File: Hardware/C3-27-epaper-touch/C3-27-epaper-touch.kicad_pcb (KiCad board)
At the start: 4 copper layers, 70.2 x 71 mm, 63 parts, among them J1 AFC24-S24FIC-00, J2 USB_C_Programming, J3 Conn_01x06, J4 Conn_01x06_Female, J5 Groove sensor, Q1 Si1308, Q2 BC817, Q3 BC817, U1 ESP32-C3-WROOM-02-N4, U2 CP2102N-A02-GQFN28R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

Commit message: C3 PCB update RES label
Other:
- board text added: "0.47Ω"
- board text removed: "4.7Ω"

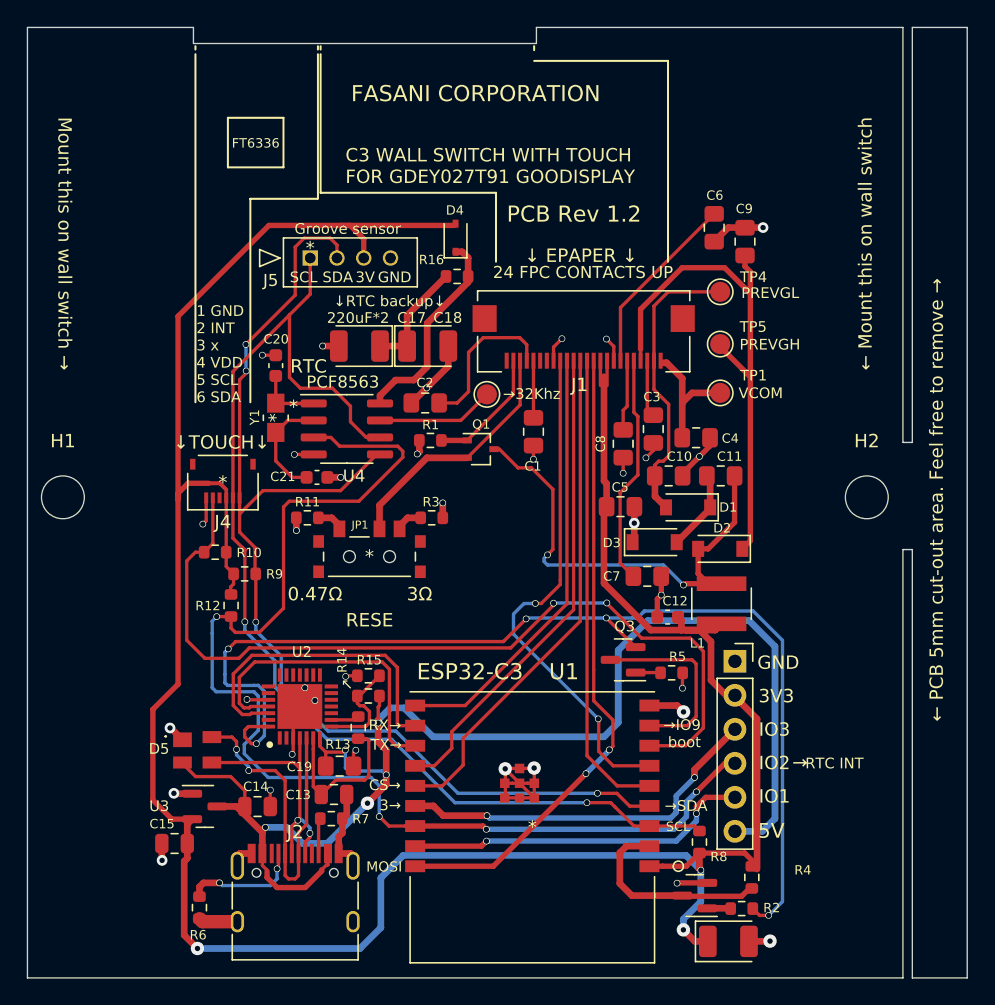
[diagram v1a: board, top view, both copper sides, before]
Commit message: Optimize deepsleep for C3 version
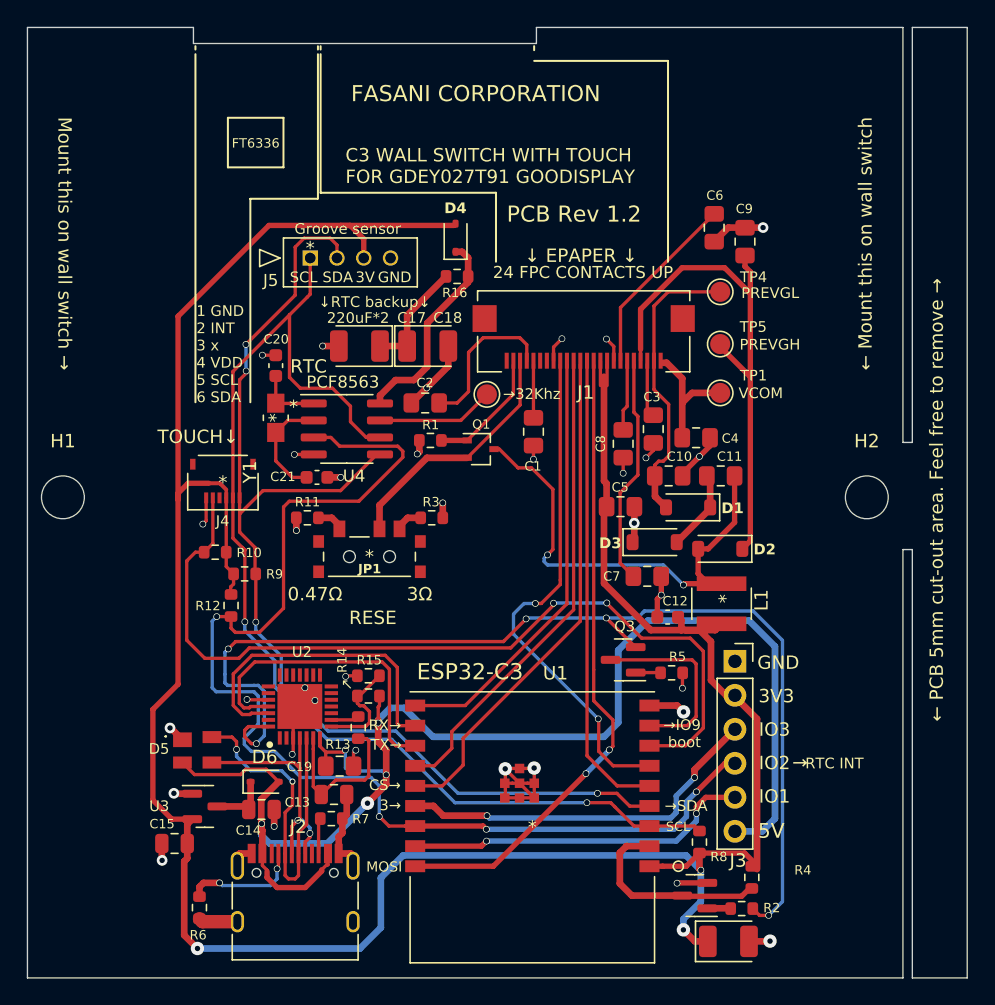
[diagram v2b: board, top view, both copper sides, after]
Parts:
- added D6: 1N5819WS, Diode_SMD:D_SOD-323, F.Cu at (122.5, 111.3)
- J1: value AFC24-S24FIC-00 -> CONN_AFC24-S24FIC-00_JUS
- U1: value ESP32-C3-WROOM-02-N4 -> IC18_ESP32-C3-WROOM-02-N4_EXP
- moved C14 0.36 mm to (122.3, 113.4)
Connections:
- C14 pad 1: VBUS -> Net-(D6-K)
- U3 pad 3: VBUS -> Net-(D6-K)
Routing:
- net Net-(D6-K): track 0.00 -> 4.04 mm
- net VBUS: track 102.6 -> 104.5 mm
- net /D-: track 26.4 -> 27.0 mm
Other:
- board text added: "TOUCH↓"
- board text removed: "↓TOUCH↓"

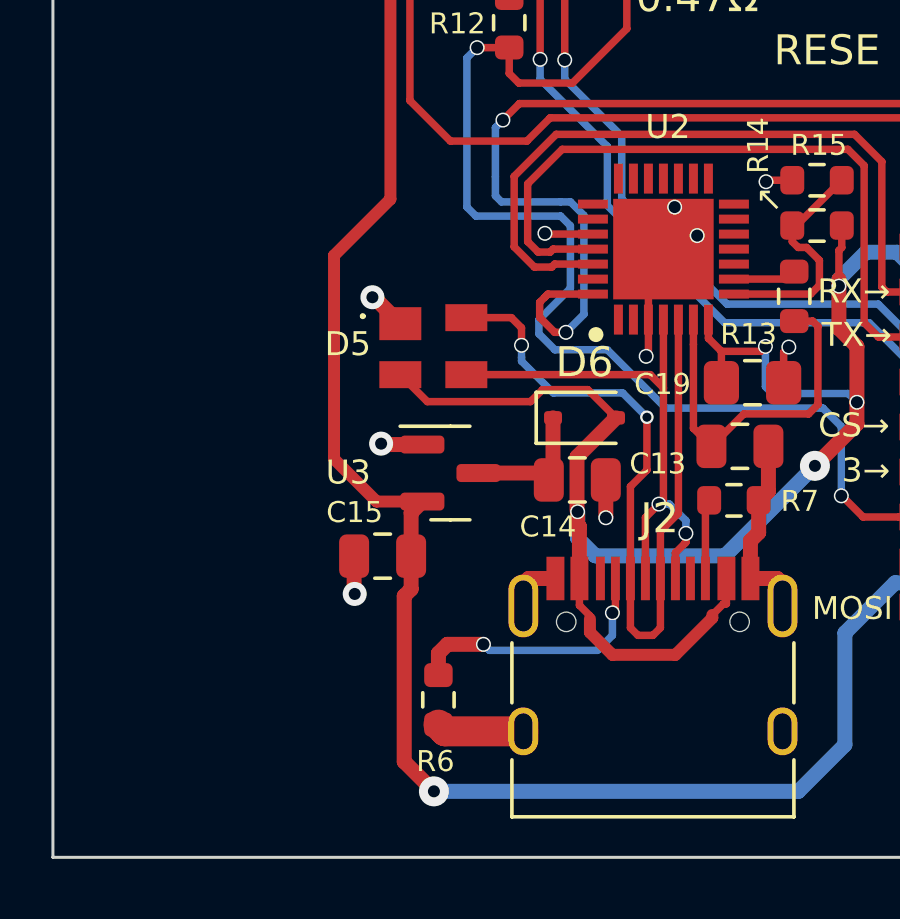
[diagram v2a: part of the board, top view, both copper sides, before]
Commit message: Switch LDO to RT9013-33GB Ref https://github.com/martinberlin/H-spi-adapters/issues/9
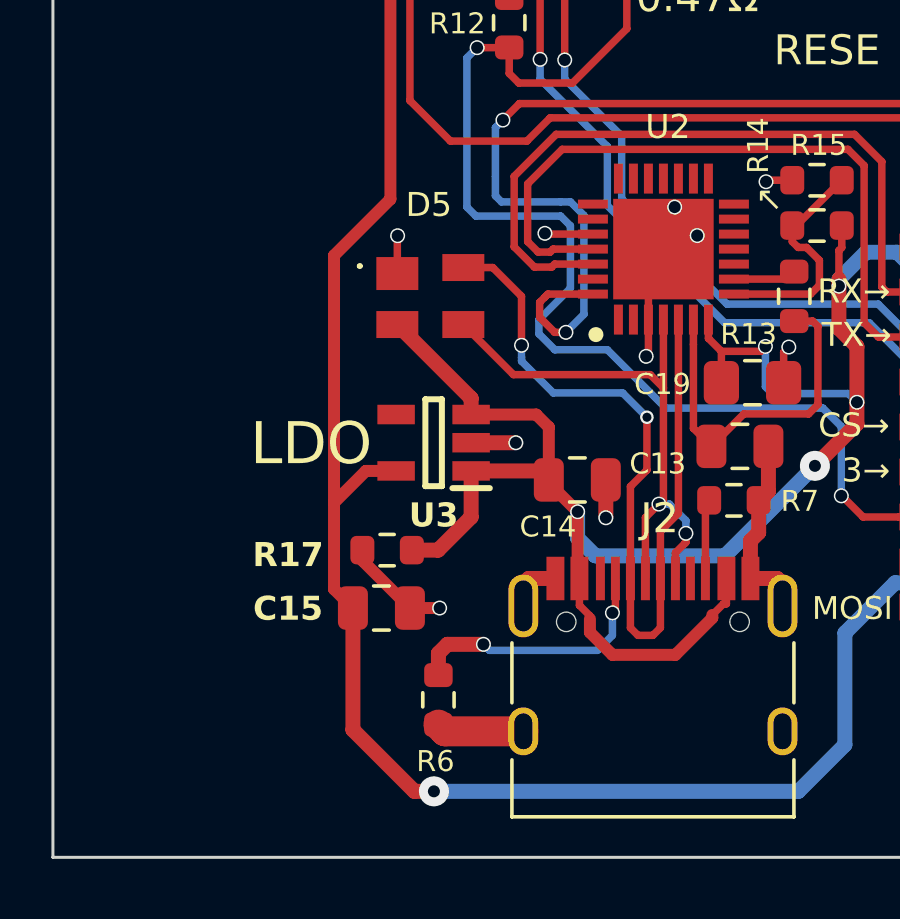
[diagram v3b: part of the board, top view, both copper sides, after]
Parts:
- removed D6: 1N5819WS, Diode_SMD:D_SOD-323
- added R17: 47K, Resistor_SMD:R_0603_1608Metric, F.Cu at (115.9, 115.8)
- J1: value CONN_AFC24-S24FIC-00_JUS -> AFC24-S24FIC-00
- U1: value IC18_ESP32-C3-WROOM-02-N4_EXP -> ESP32-C3-WROOM-02-N4
- U3: value MCP1700-3302E_SOT23 -> RT9013-33GB; footprint Package_TO_SOT_SMD:SOT-23 -> footprint:RT9013-33GB
- moved C15 1.73 mm to (115.8, 117.7), turned to 0 degrees
- moved D5 1.67 mm to (117.4, 107.3)
- moved U3 1.15 mm to (117.5, 112.2), turned to 180 degrees
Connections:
- C14 pad 1: Net-(D6-K) -> VBUS
- U3 pad 1: GND -> VBUS
- U3 pad 2: +3V3 -> GND
- U3 pad 3: Net-(D6-K) -> VBUS
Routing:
- net VBUS: track 104.5 -> 109.5 mm
- net Net-(D6-K): track 4.04 -> 0.00 mm
- net GND: track 76.1 -> 78.4 mm
- net +3V3: track 202.7 -> 204.2 mm
- net /D-: track 27.0 -> 28.4 mm
- net /D+: track 18.8 -> 19.6 mm
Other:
- board text added: "LDO"
